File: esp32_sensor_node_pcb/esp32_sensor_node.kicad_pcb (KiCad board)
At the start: 4 copper layers, 49.9 x 59.9 mm, 28 parts, among them J1 Conn_02x10_Odd_Even, Q1 2N7002K, SW1 SW_DIP_x01, U1 HT7833, U2 ESP32-WROOM-E, U3 MAX3483AEASA+

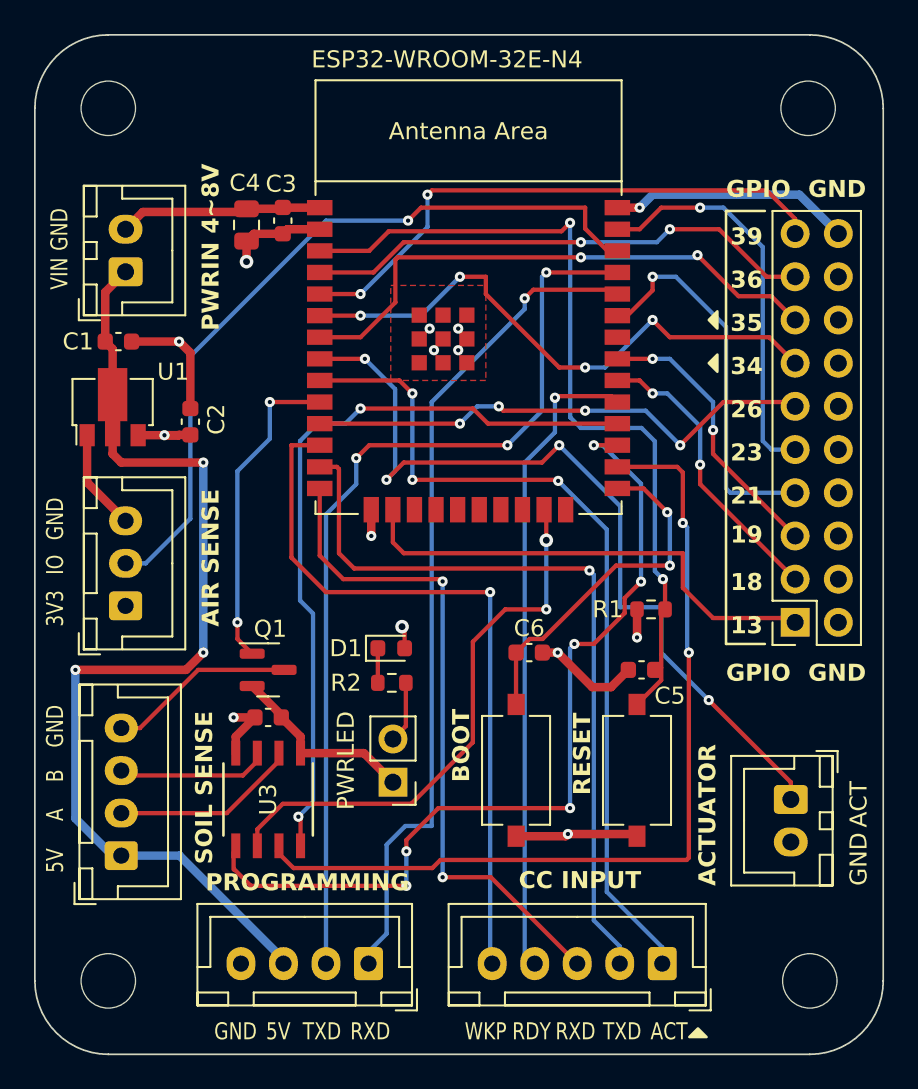
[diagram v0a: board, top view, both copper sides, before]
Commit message: Add 3v3 outputs on header. Shift labels for alignment. Add board names on back.
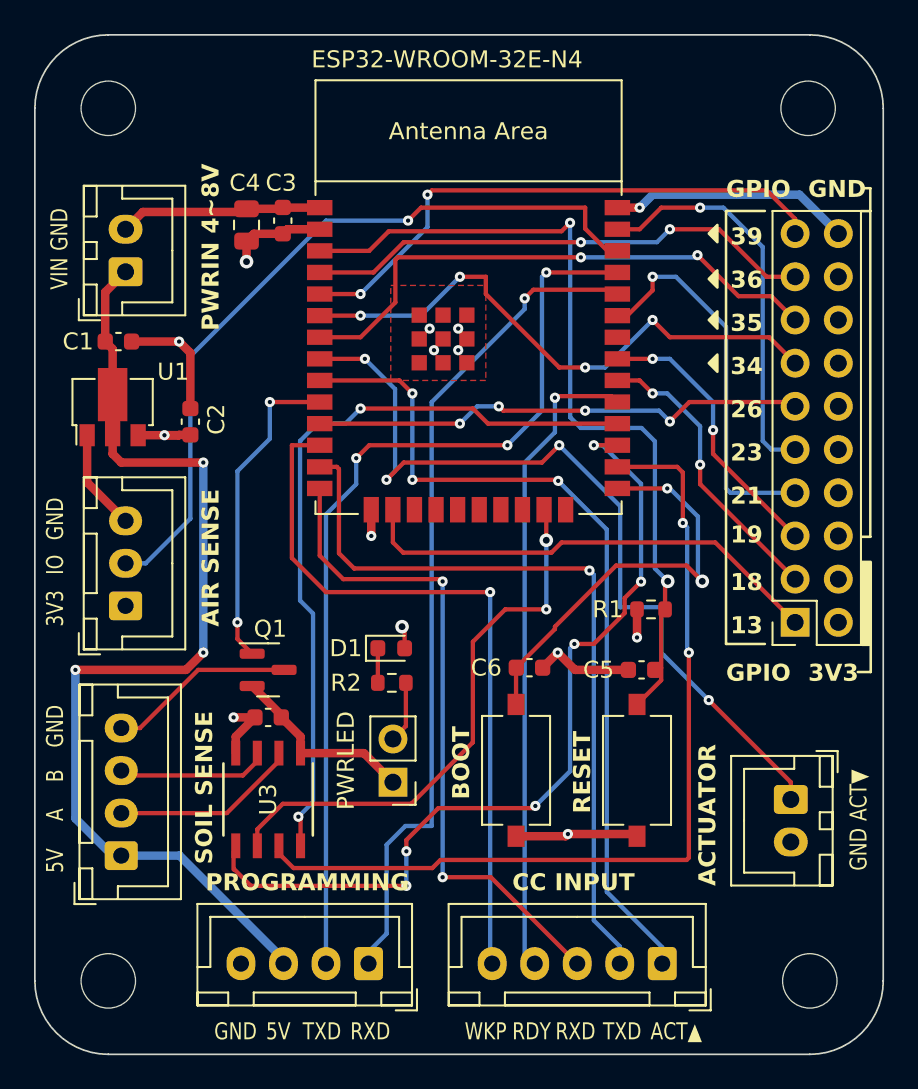
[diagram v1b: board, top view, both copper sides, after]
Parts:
- moved C6 0.89 mm to (49.1, 57.3)
- renumbered BOOT to SW2
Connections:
- J1 pad 2: GND -> +3.3V
- J1 pad 4: GND -> +3.3V
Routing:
- net GPIO0/BOOT: track 21.0 -> 25.4 mm
- net Net-(U2-GPIO16): track 51.2 -> 49.9 mm
- net GPIO26: track 30.1 -> 29.0 mm
- net GPIO13: track 28.4 -> 27.7 mm
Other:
- board text added: "ACT▲"
- board text added: "ACT▼"
- board text added: "ECE496 CC Sense/Actuate Board REV 1 - DEC 2023"
- board text added: "M. Qureshi & J. Xu"
- board text removed: "ACT"

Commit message: Change LDO HT7833 -> SPX3819, reroute, relabel. Generate BOM testing.
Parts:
- R2: value 4.7K -> 2.2K
- U1: value HT7833 -> SPX3819M5-L-3-3; footprint Package_TO_SOT_SMD:SOT-89-3 -> Package_TO_SOT_SMD:SOT-23-5
- moved U1 0.37 mm to (24.7, 42.0), turned to 0 degrees
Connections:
- U1 pad 1: GND -> +5V
- U1 pad 2: +5V -> GND
- U1 pad 3: +3.3V -> +5V
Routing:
- net +3.3V: track 16.5 -> 28.6 mm, vias 5 -> 4
- net GND: track 64.5 -> 59.6 mm, vias 9 -> 10
- net +5V: track 60.2 -> 62.1 mm
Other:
- board text added: "PWRIN 4~16V"
- board text removed: "PWRIN 4~8V"

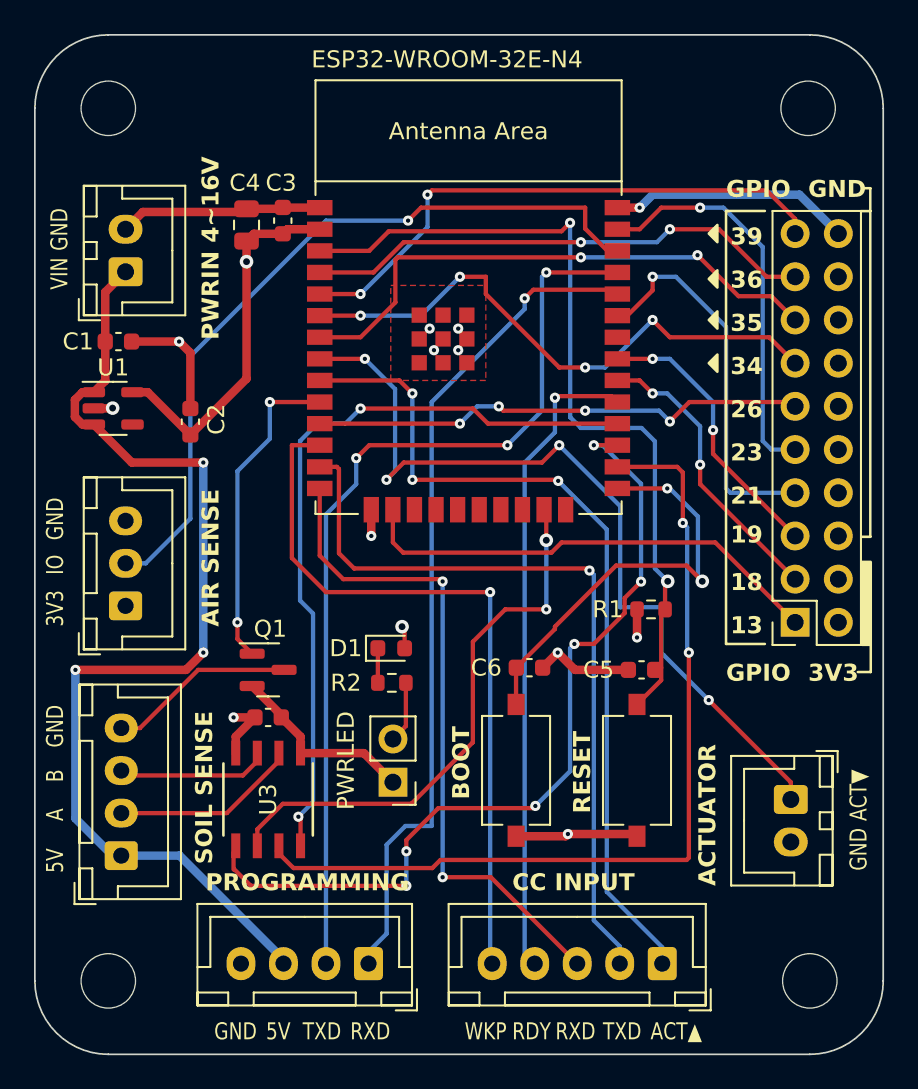
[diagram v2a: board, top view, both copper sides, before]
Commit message: Changed 2.2uF cap to 0805. Added power flag on 5V and not-connected for BP pin. Changed all vias to 0.3mm hole size. Changed programming interface to 2.54mm PIN headers.
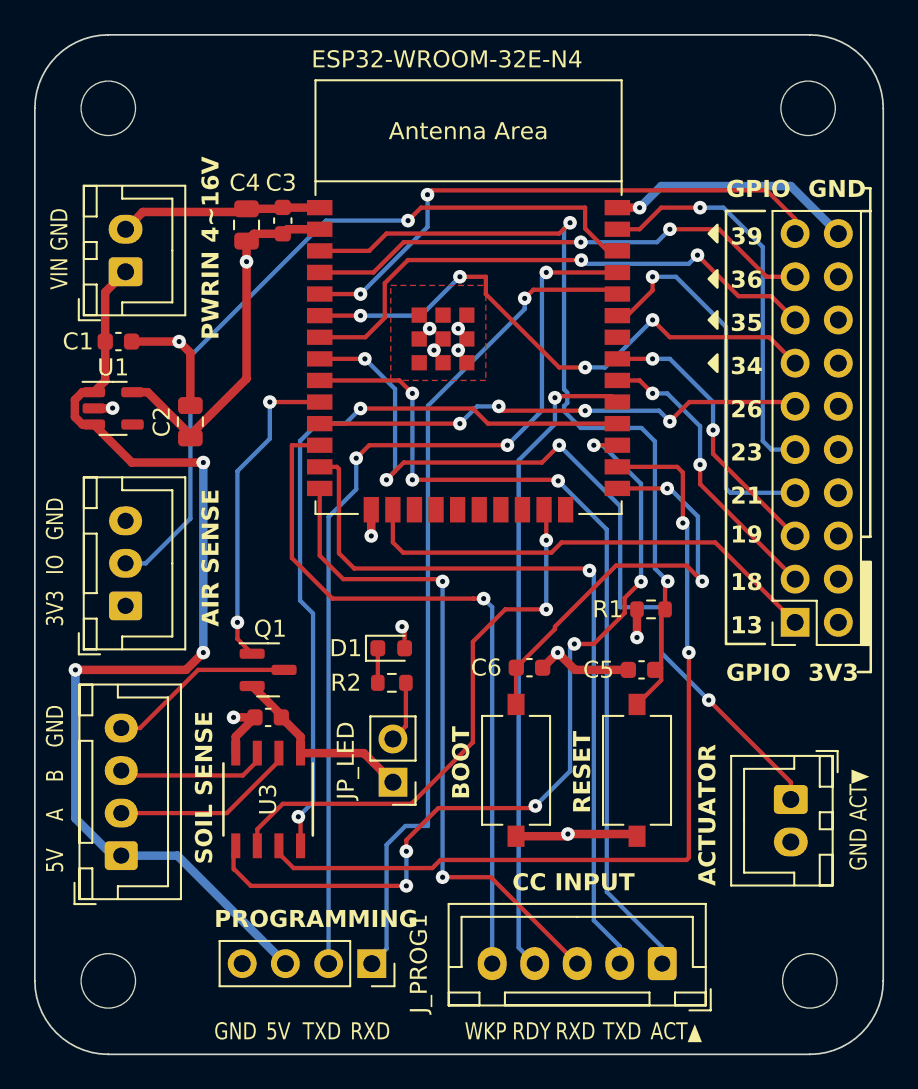
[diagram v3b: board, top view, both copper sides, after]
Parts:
- C2: footprint Capacitor_SMD:C_0603_1608Metric -> Capacitor_SMD:C_0805_2012Metric
- J_PROG1: footprint Connector_JST:JST_XH_B4B-XH-A_1x04_P2.50mm_Vertical -> Connector_PinSocket_2.54mm:PinSocket_1x04_P2.54mm_Vertical
- moved J_PROG1 0.19 mm to (39.9, 74.7), turned to -90 degrees
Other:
- board text added: "JP_LED"
- board text removed: "PWRLED"

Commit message: Removed reference designators on the silk screen
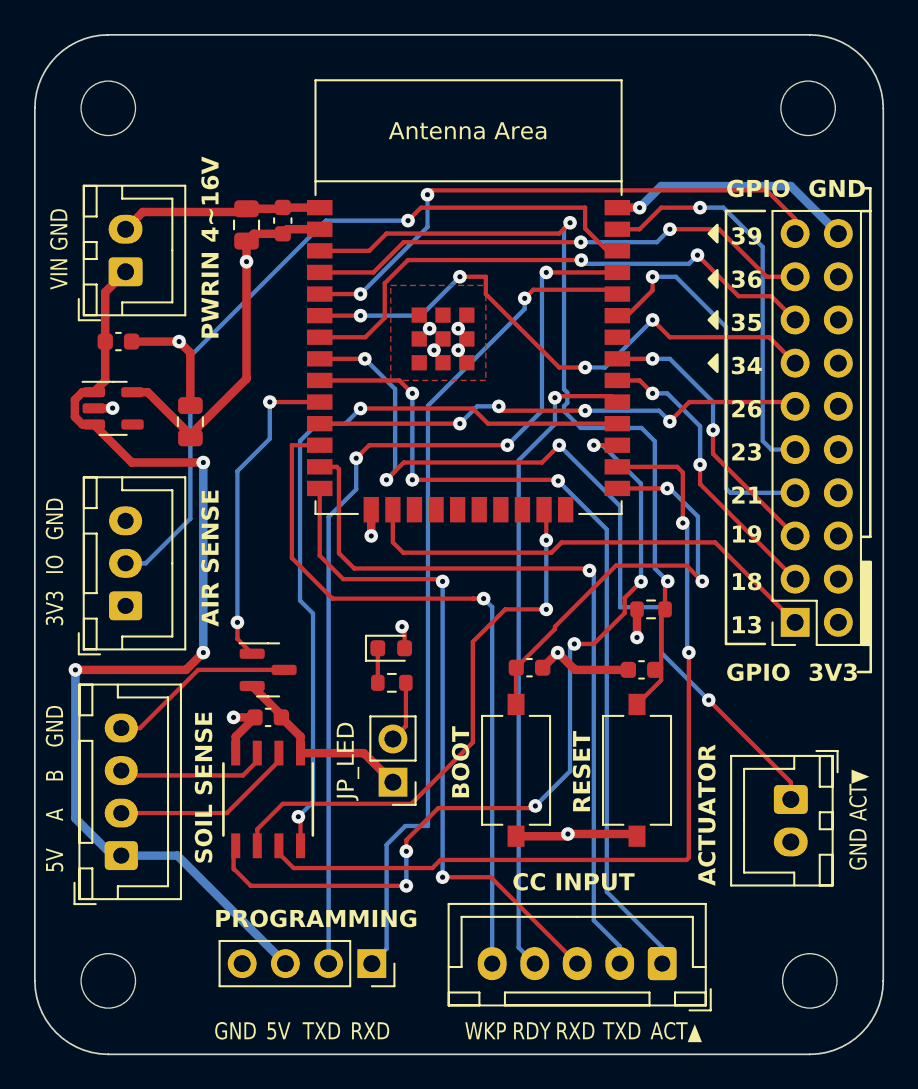
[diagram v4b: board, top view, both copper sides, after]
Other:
- board text removed: "ESP32-WROOM-32E-N4"
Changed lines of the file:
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@@
     (property "ki_keywords" "capacitor cap")
     (attr smd)
-    (fp_text reference "C6" (at -2.54 0) (layer "F.SilkS")
+    (fp_text reference "C6" (at -2.54 0) (layer "F.SilkS") hide
         (effects (font (size 1 1) (thickness 0.15)))
     )
@@
     (property "ki_keywords" "R res resistor")
     (attr smd)
-    (fp_text reference "R2" (at 2.703 0) (layer "F.SilkS")
+    (fp_text reference "R2" (at 2.703 0) (layer "F.SilkS") hide
         (effects (font (size 1 1) (thickness 0.15)))
     )
@@
     (property "ki_keywords" "capacitor cap")
     (attr smd)
-    (fp_text reference "C4" (at 2.474 -0.1 180) (layer "F.SilkS")
+    (fp_text reference "C4" (at 2.474 -0.1 180) (layer "F.SilkS") hide
         (effects (font (size 1 1) (thickness 0.15)))
     )
@@
     (property "ki_keywords" "capacitor cap")
     (attr smd)
-    (fp_text reference "C5" (at 2.526 0 180) (layer "F.SilkS")
+    (fp_text reference "C5" (at 2.526 0 180) (layer "F.SilkS") hide
         (effects (font (size 1 1) (thickness 0.15)))
     )
@@
     (property "ki_keywords" "connector")
     (attr through_hole)
-    (fp_text reference "J_PROG1" (at 0 -2.77 90) (layer "F.SilkS")
+    (fp_text reference "J_PROG1" (at 0 -2.77 90) (layer "F.SilkS") hide
         (effects (font (size 1 1) (thickness 0.15)))
     )
@@
     (property "ki_keywords" "REGULATOR LDO 3.3V")
     (attr smd)
-    (fp_text reference "U1" (at 0 -2.4) (layer "F.SilkS")
+    (fp_text reference "U1" (at 0 -2.4) (layer "F.SilkS") hide
         (effects (font (size 1 1) (thickness 0.15)))
     )
@@
     (property "ki_keywords" "capacitor cap")
     (attr smd)
-    (fp_text reference "C1" (at -2.373 0) (layer "F.SilkS")
+    (fp_text reference "C1" (at -2.373 0) (layer "F.SilkS") hide
         (effects (font (size 1 1) (thickness 0.15)))
     )
@@
     (property "ki_keywords" "capacitor cap")
     (attr smd)
-    (fp_text reference "C2" (at 0 -1.68 90) (layer "F.SilkS")
+    (fp_text reference "C2" (at 0 -1.68 90) (layer "F.SilkS") hide
         (effects (font (size 1 1) (thickness 0.15)))
     )
@@
     (property "ki_keywords" "N-Channel MOSFET")
     (attr smd)
-    (fp_text reference "Q1" (at 0.127 -2.413) (layer "F.SilkS")
+    (fp_text reference "Q1" (at 0.127 -2.413) (layer "F.SilkS") hide
         (effects (font (size 1 1) (thickness 0.15)))
     )
@@
     (property "ki_keywords" "capacitor cap")
     (attr smd)
-    (fp_text reference "C3" (at 2.22 -0.1 180) (layer "F.SilkS")
+    (fp_text reference "C3" (at 2.22 -0.1 180) (layer "F.SilkS") hide
         (effects (font (size 1 1) (thickness 0.15)))
     )
@@
     (property "ki_keywords" "MAX3483AEASA+")
     (attr smd)
-    (fp_text reference "U3" (at 0 0 90 unlocked) (layer "F.SilkS")
+    (fp_text reference "U3" (at 0 0 90 unlocked) (layer "F.SilkS") hide
         (effects (font (size 1 1) (thickness 0.15)))
     )
@@
     (property "ki_keywords" "LED diode")
     (attr smd)
-    (fp_text reference "D1" (at -2.6685 0) (layer "F.SilkS")
+    (fp_text reference "D1" (at -2.6685 0) (layer "F.SilkS") hide
         (effects (font (size 1 1) (thickness 0.15)))
     )
@@
     (property "ki_keywords" "R res resistor")
     (attr smd)
-    (fp_text reference "R1" (at -2.54 0 180) (layer "F.SilkS")
+    (fp_text reference "R1" (at -2.54 0 180) (layer "F.SilkS") hide
         (effects (font (size 1 1) (thickness 0.15)))
     )
@@
     (effects (font (size 1 1) (thickness 0.25) bold) (justify left bottom))
   )
-  (gr_text "ESP32-WROOM-32E-N4" (at 36.322 22.098) (layer "F.SilkS")
-    (effects (font (size 1 1) (thickness 0.15)) (justify left bottom))
-  )
   (gr_text "GND" (at 65.532 29.718) (layer "F.SilkS" knockout)

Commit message: Add copyright & transfer vias. Checked ERC and DRC.
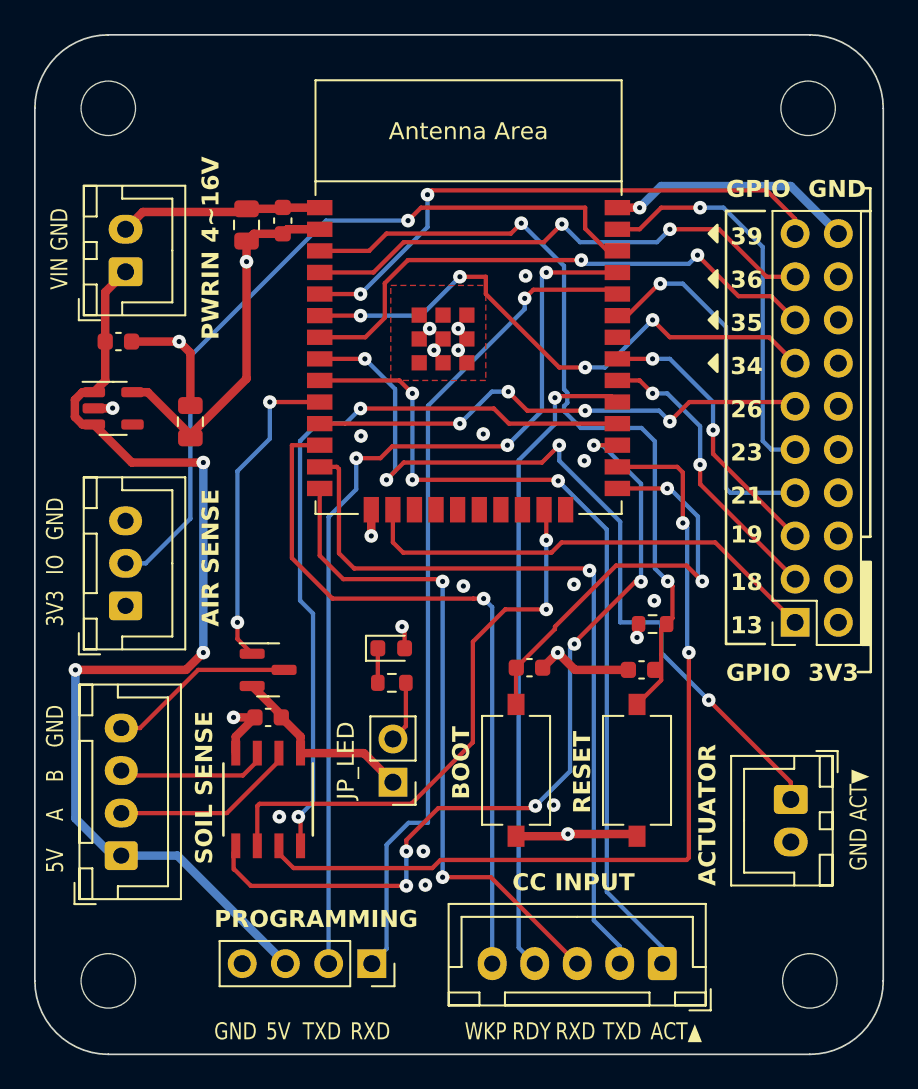
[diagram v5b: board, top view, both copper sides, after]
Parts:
- moved R1 0.87 mm to (56.4, 54.7)
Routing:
- net RESET: track 49.1 -> 47.6 mm
- net GPIO36: track 30.2 -> 31.0 mm
- net +3.3V: track 28.6 -> 27.8 mm
- net GPIO21: track 22.1 -> 21.3 mm
- net RS485_*RE: track 32.5 -> 33.3 mm
- net GPIO26: track 29.0 -> 29.7 mm
- net GND: vias 10 -> 21
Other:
- board text added: "Copyright © 2023 UofT Network Research Lab"
